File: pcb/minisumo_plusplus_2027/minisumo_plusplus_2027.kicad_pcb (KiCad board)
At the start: 2 copper layers, 211.6 x 112.8 mm, 51 parts, among them J3 Start Module - Conn_01x04_Pin, J5 Conn_01x10_Pin, SW1 SW_SPDT, U3 ESP32-C6-SuperMini

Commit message: pcb now with 2a buck boost MT3608, updated footprints incl motor driver @2.54 pins int1-4, and c6 && 3d with updated buck boost along with pcb!
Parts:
- removed the A1 at (149.7, 101.8)
- removed the A1 at (230.3, 126.2)
- removed the A1 at (230.2, 93.2)
- removed the A1 at (149.7, 68.8)
- removed the A1 at (230.2, 60.2)
- removed the A1 at (149.7, 134.8)
- removed A2 (x7): ~, minisumo_plusplus_2027:XL6009 4A Boost Converter Step Up Adjustable 15W 5-32V to 5-50V DC-DC Power Supply Module LM2577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
- removed the J3 at (230.3, 123.8)
- removed the J3 at (149.7, 137.2)
- removed the J3 at (230.2, 57.8)
- removed the J3 at (149.7, 71.2)
- removed the J3 at (149.7, 104.2)
- removed the J3 at (230.2, 90.8)
- removed the J5 at (226.4, 112.3)
- removed the J5 at (153.5, 82.7)
- removed the J5 at (226.5, 145.3)
- removed the J5 at (153.5, 115.7)
- removed the J5 at (226.4, 79.3)
- removed the J5 at (153.5, 49.7)
- removed REF** (x2): Stripboard_3x19_P2.54mm, minisumo_plusplus_2027:Stripboard_3x19_P2.54mm
- removed the SW1 at (196.8, 87.2)
- removed the SW1 at (183.1, 74.8)
- removed the SW1 at (183.1, 140.8)
- removed the SW1 at (183.1, 107.8)
- removed the SW1 at (196.9, 120.2)
- removed the SW1 at (196.8, 54.2)
- removed the U2 at (183.2, 144.2)
- removed the U2 at (196.7, 50.8)
- removed the U2 at (196.7, 83.8)
- removed the U2 at (196.7, 116.8)
- removed the U2 at (183.2, 78.2)
- removed the U2 at (183.2, 111.2)
- removed the U3 at (177.6, 137.3)
- removed the U3 at (202.3, 57.7)
- removed the U3 at (202.3, 123.7)
- removed the U3 at (202.3, 90.7)
- removed the U3 at (177.6, 104.3)
- removed the U3 at (177.6, 71.3)
- added A3: ~, minisumo_plusplus_2027:MT3608 DC-DC Boost Module – 28V 2A Step-Up Power Module, B.Cu at (12.5, 22.7)
- A1: footprint minisumo_plusplus_2027:Mini_L298N_2_Channel_H_Bridge_DC_Motor_Driver_Board_with_MX1508-special_silk -> minisumo_plusplus_2027:Mini_L298N_2_Channel_H_Bridge_DC_Motor_Driver_Board_with_MX1508-2.54_int1-4-special_silk
- U2: footprint minisumo_plusplus_2027:battery cr123 3.7v with contacts for 18650_special_silk -> BBQ_Library:battery cr123 3.7v with contacts for 18650
- moved A1 47.0 mm to (33.3, 11.9)
- moved J5 45.5 mm to (31.5, 31.3)
- moved U3 45.5 mm to (7.34, 9.72)
- moved J3 45.5 mm to (35.3, 9.81)
- moved SW1 45.5 mm to (1.88, 6.21)
- moved U2 45.5 mm to (1.75, 2.81)
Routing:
- net 3v3: track 528.6 -> 75.8 mm, vias 14 -> 2
- net /3v7 (>3v3 & <5v): track 256.1 -> 19.1 mm
- net START Kill - not mandatory for sumo: track 198.6 -> 20.6 mm
- net Net-(A1-INT1): track 196.9 -> 26.4 mm
- net IR Rear: track 198.0 -> 28.3 mm, vias 21 -> 3
- net Net-(A1-INT2): track 180.8 -> 23.4 mm
- net IR Front: track 177.1 -> 27.3 mm, vias 7 -> 1
- net /9v: track 146.2 -> 7.62 mm, vias 7 -> 0
- net Net-(A1-INT3): track 144.3 -> 20.6 mm, vias 7 -> 1
- net START Start: track 132.5 -> 18.9 mm
- net GND: track 98.7 -> 14.1 mm
- net Net-(A1-INT4): track 94.8 -> 18.1 mm, vias 7 -> 1
- net Net-(A1-gnd): track 51.2 -> 10.1 mm
- net US Echo Tx: track 40.9 -> 5.85 mm
- net US Trigger Rx: track 40.9 -> 5.85 mm
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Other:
- board size 211.6 x 112.8 mm -> 240.5 x 148 mm
- board text added: "BUCK BOOST MT3608"
- board text added: "v260914b"
- board text removed: "BUCK BOOST LM2596"
- board text removed: "GND /IN-"
- board text removed: "IN+"
- board text removed: "SPONSOR LOGO HERE"
- board text removed: "v260903"

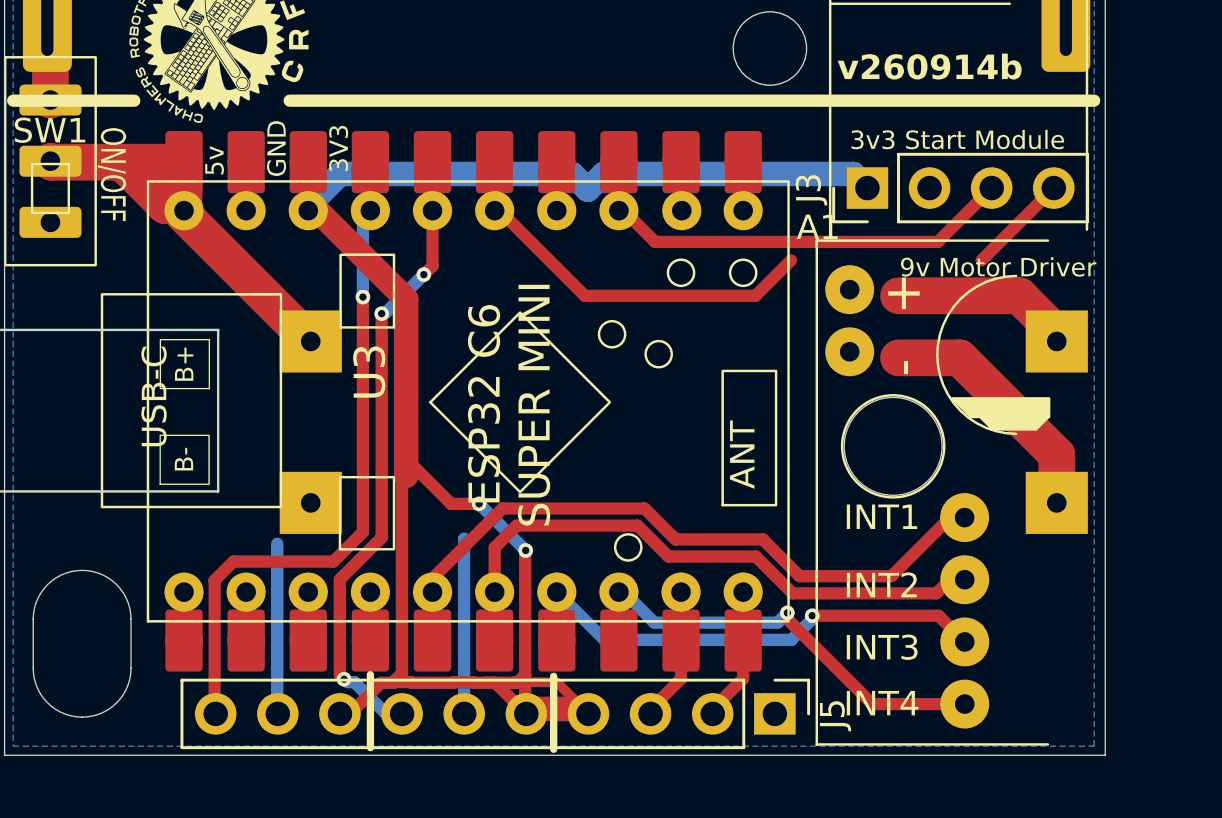
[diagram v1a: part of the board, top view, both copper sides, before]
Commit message: pcb - fixed traces incl around antenna a gnd strip outside keepout on A side with stitching vias and no gnd plane on b side acc to espressif instructions
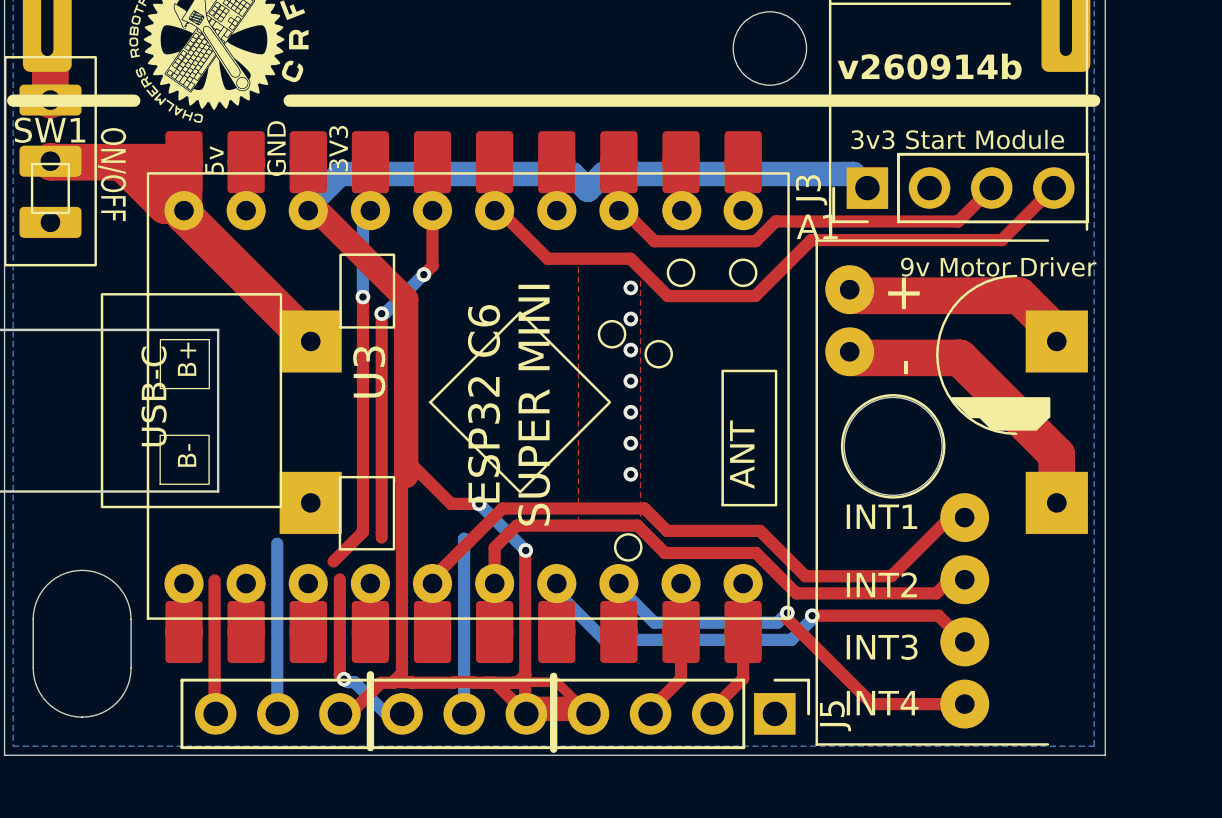
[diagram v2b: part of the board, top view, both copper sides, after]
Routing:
- net START Kill - not mandatory for sumo: track 20.6 -> 28.4 mm
- net IR Front: track 27.3 -> 22.1 mm
- net IR Rear: track 28.3 -> 25.9 mm
- net Net-(A1-gnd): track 10.1 -> 12.2 mm
- net /9v: track 7.62 -> 9.21 mm
- net GND: vias 0 -> 7
- added copper zone on F.Cu, net GND

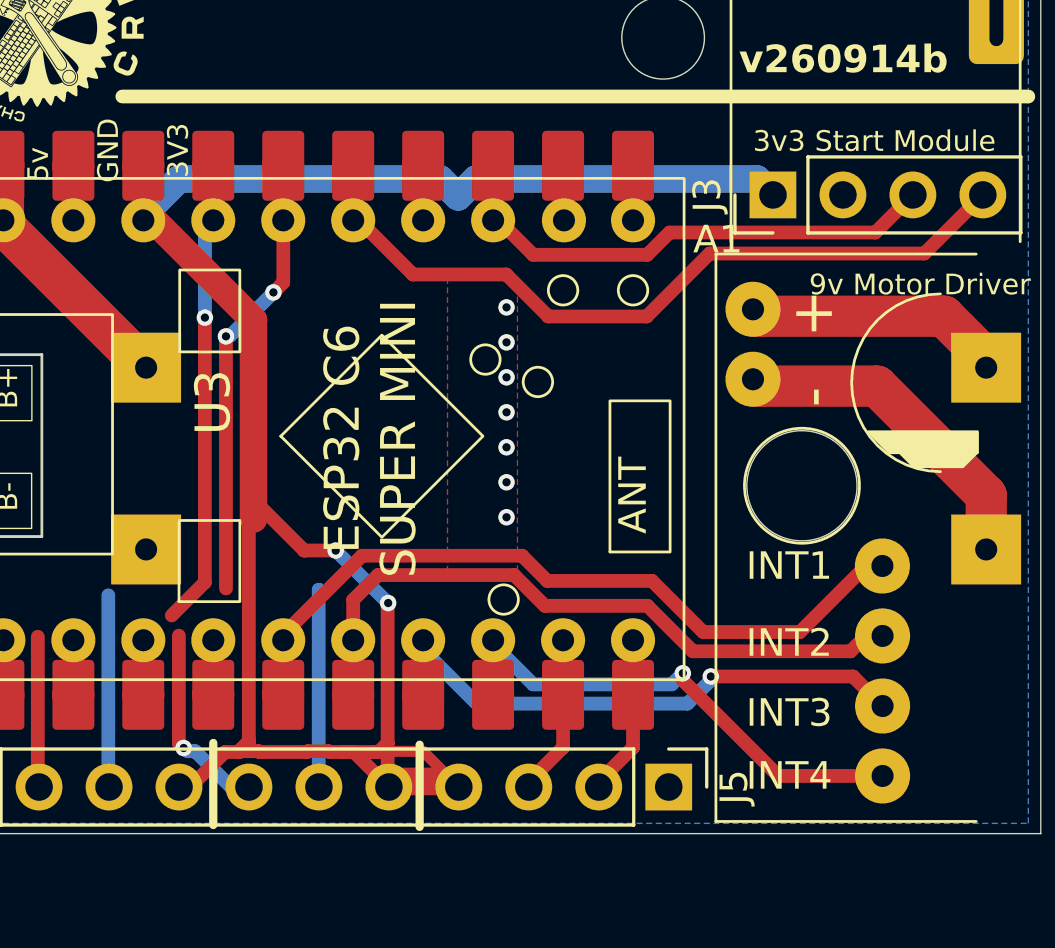
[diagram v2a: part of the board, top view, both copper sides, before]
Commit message: pcb .. fixed a 3v3 trace near battery cut
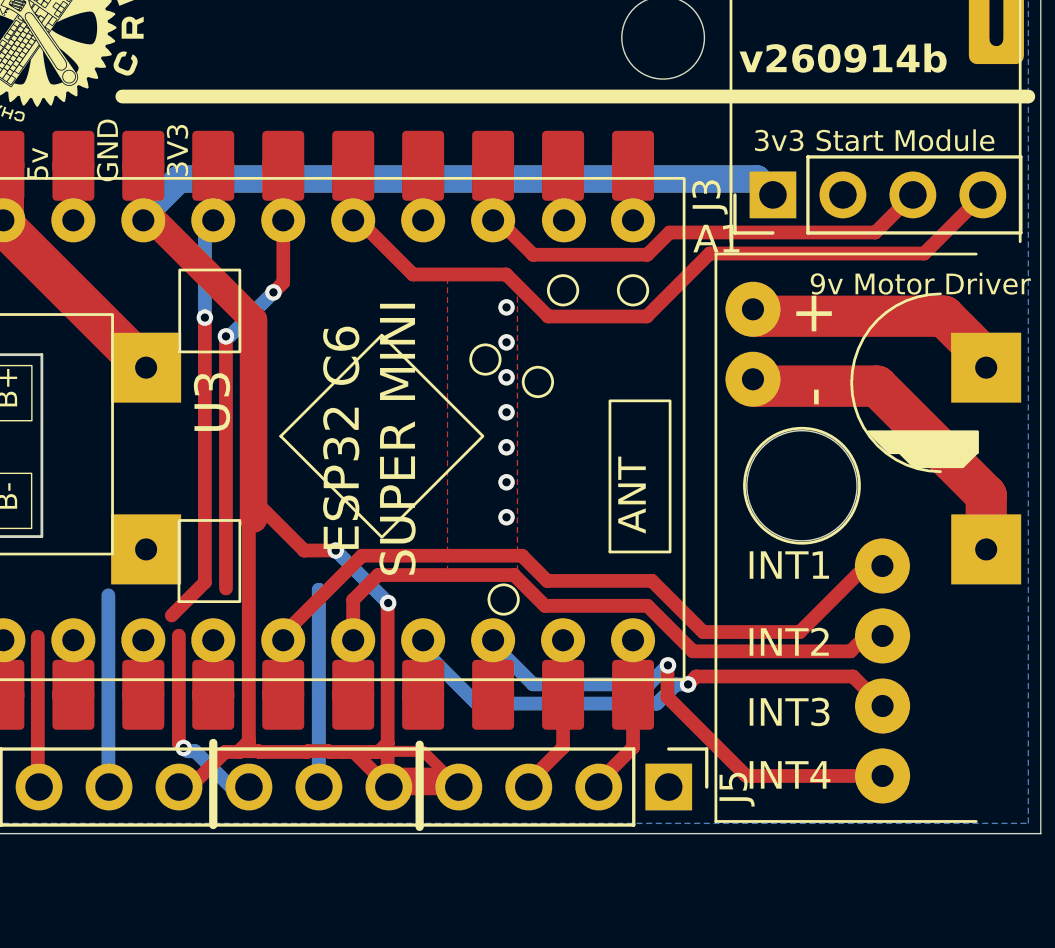
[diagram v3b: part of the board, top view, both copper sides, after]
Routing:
- net Net-(A1-INT4): track 18.1 -> 18.9 mm
- net 3v3: track 75.8 -> 75.3 mm

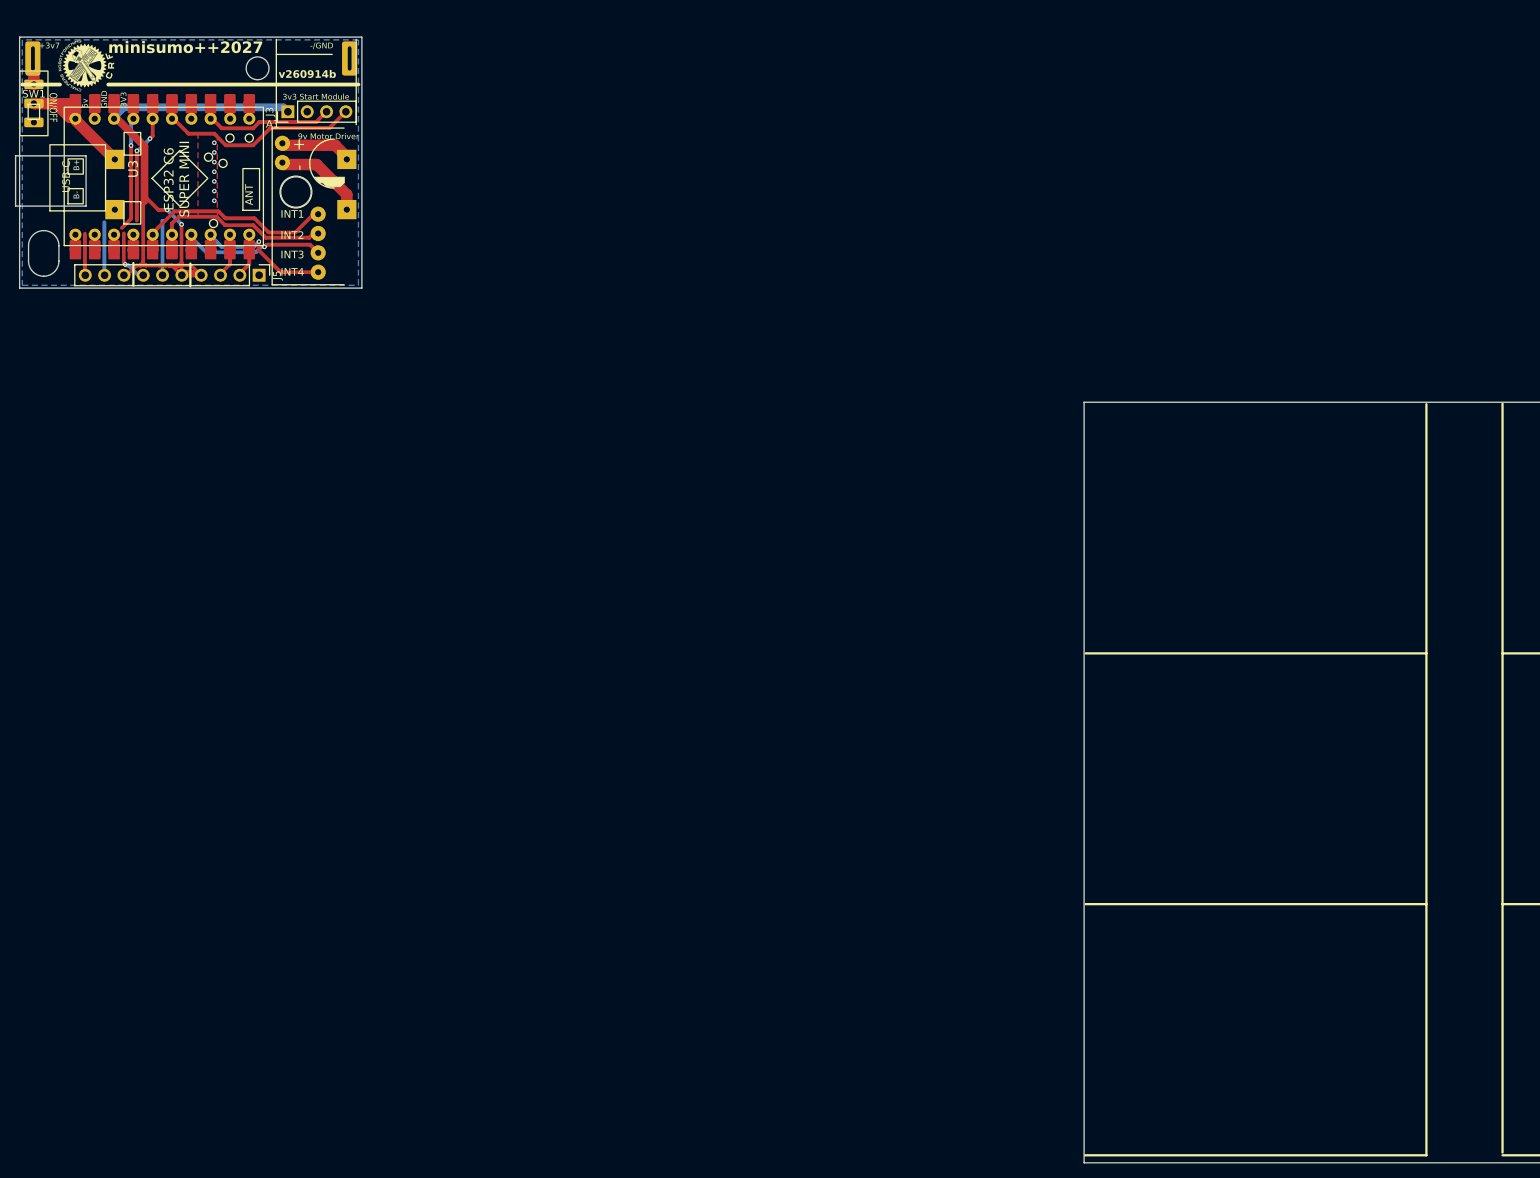
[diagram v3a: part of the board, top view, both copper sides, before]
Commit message: pcb - updated footprints w 3d and fixed broken traces && 3d - redid assemblies they were a bit of a mess.
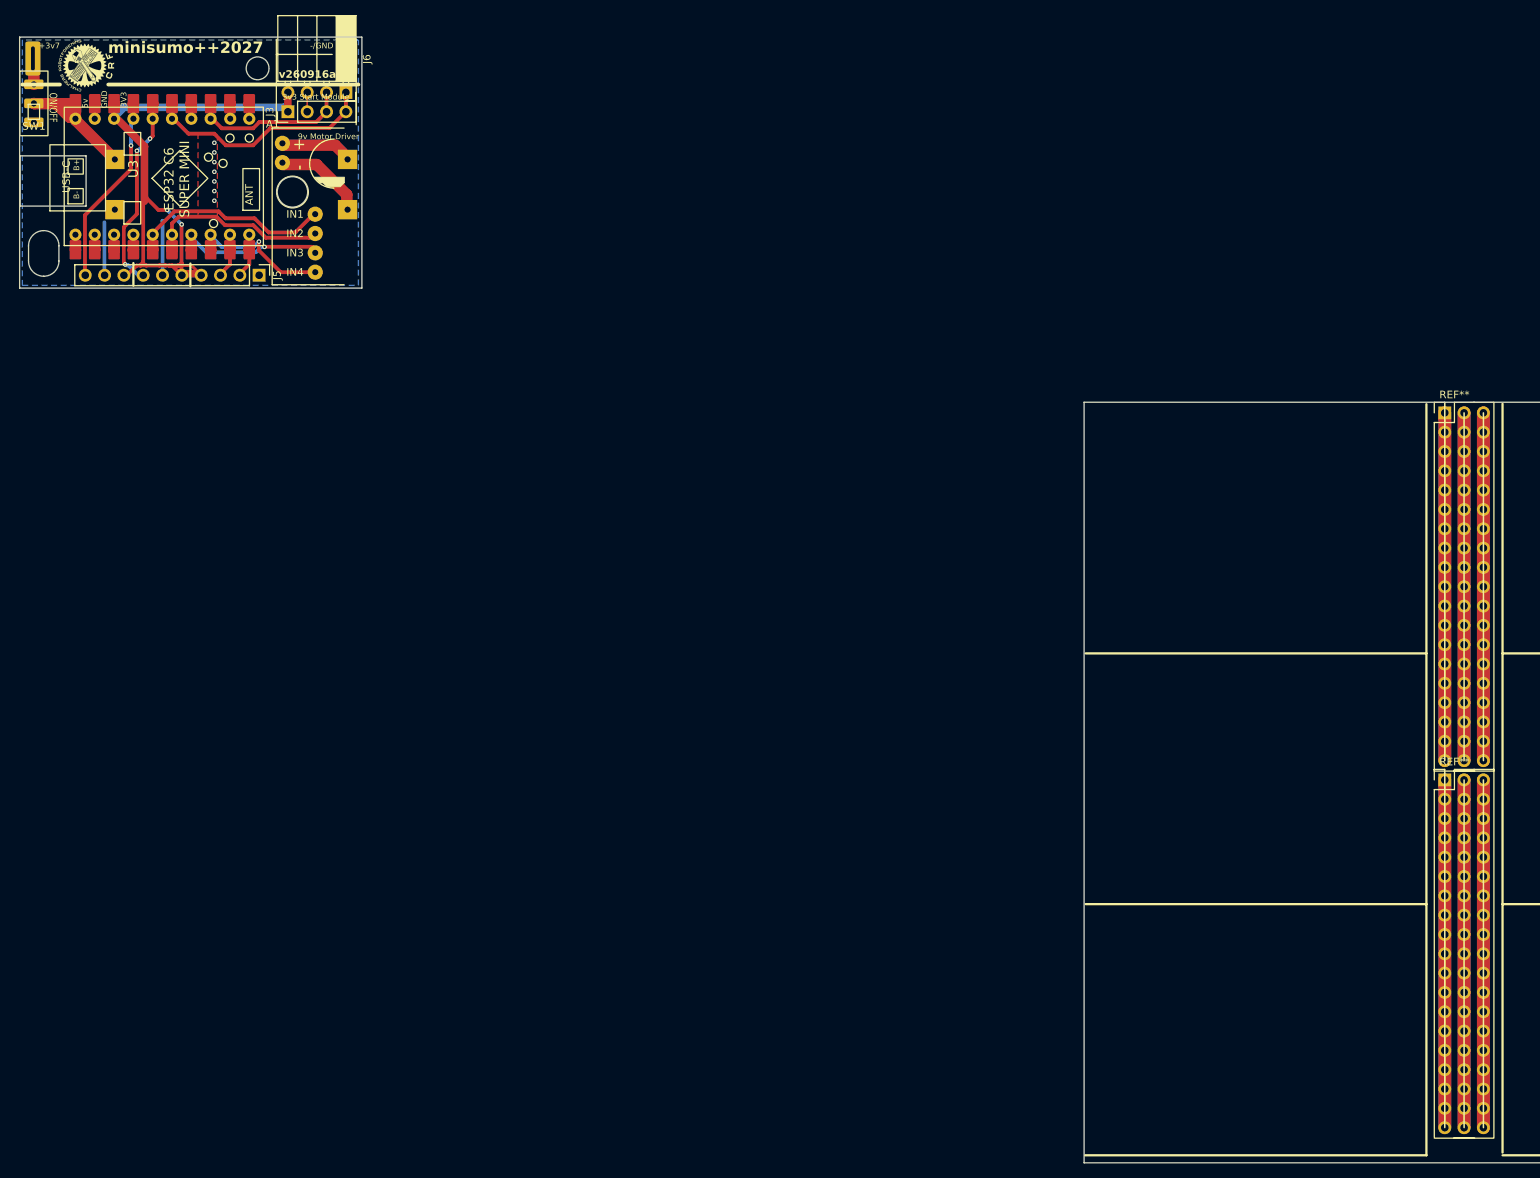
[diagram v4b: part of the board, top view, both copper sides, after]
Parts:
- added J6: Start Module - Conn_01x04_Pin, Connector_PinSocket_2.54mm:PinSocket_1x04_P2.54mm_Horizontal, F.Cu at (42.9, 7.27)
- added REF**: Stripboard_3x19_P2.54mm, minisumo_plusplus_2027:Stripboard_3x19_P2.54mm, F.Cu at (187.4, 49.4)
- added REF**: Stripboard_3x19_P2.54mm, minisumo_plusplus_2027:Stripboard_3x19_P2.54mm, F.Cu at (187.4, 97.7)
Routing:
- net IR Front: track 22.1 -> 24.9 mm
- net START Start: track 18.9 -> 21.4 mm
- net START Kill - not mandatory for sumo: track 28.4 -> 30.9 mm
- net GND: track 14.1 -> 16.6 mm
- net 3v3: track 75.3 -> 77.8 mm
- net IR Rear: track 25.9 -> 28.3 mm
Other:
- board size 240.5 x 148 mm -> 240 x 148 mm
- board text added: "v260916a"
- board text removed: "v260914b"
